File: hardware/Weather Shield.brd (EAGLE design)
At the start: 53.3 x 59.7 mm, 44 parts, among them Q1 BSS138, Q2 BSS138, U1 ARDUINO_R3_SHIELD, U2 3.3V MIC5219, U4 MPL3115A2LGA8, U5 HTU21D, U7 GP-635T, U8 TEMT6000

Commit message: Added analog sense on VIN/Batt level.
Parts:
- added R7: 1K, SparkFun:0603-RES
- added R8: 3.9K, SparkFun:0603-RES
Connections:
- new net BATT_LVL: R7.1, R8.2, U1.A2
- net GND: now also R7.2
- net RAW: now also R8.1
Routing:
- net BATT_LVL: track 0.00 -> 48.5 mm, vias 0 -> 1
- net RAW: track 42.1 -> 46.3 mm
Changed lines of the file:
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@@
 <element name="R16" library="SparkFun" package="0603-RES" value="1K" x="29.21" y="39.37" rot="R180"/>
 <element name="LOGO2" library="SparkFun-Aesthetics" package="SFE_LOGO_NAME_FLAME_.1" value="SFE_LOGO_NAME_FLAME.1_INCH" x="20.828" y="3.048"/>
+<element name="R7" library="SparkFun" package="0603-RES" value="1K" x="40.64" y="20.32" rot="R90"/>
+<element name="R8" library="SparkFun" package="0603-RES" value="3.9K" x="38.1" y="20.32" rot="R270"/>
 </elements>
 <signals>
@@
 <via x="30.48" y="34.29" extent="1-16" drill="0.508"/>
 <via x="21.59" y="27.94" extent="1-16" drill="0.508"/>
+<contactref element="R7" pad="2"/>
 </signal>
 <signal name="STAT2">
@@
 <wire x1="27.9701" y1="20" x2="30.16" y2="20" width="0.508" layer="1"/>
 <wire x1="30.16" y1="20" x2="30.61" y2="20.45" width="0.508" layer="1"/>
+<contactref element="R8" pad="1"/>
+<wire x1="34.29" y1="20.32" x2="35.56" y2="20.32" width="0.254" layer="1"/>
+<wire x1="38.1" y1="21.17" x2="36.41" y2="21.17" width="0.254" layer="1"/>
+<wire x1="36.41" y1="21.17" x2="35.56" y2="20.32" width="0.254" layer="1"/>
 </signal>
 <signal name="RXI">
@@
 <wire x1="30.06" y1="44.03" x2="33.02" y2="46.99" width="0.254" layer="1"/>
 </signal>
+<signal name="BATT_LVL">
+<contactref element="R8" pad="2"/>
+<contactref element="R7" pad="1"/>
+<contactref element="U1" pad="A2"/>
+<wire x1="50.8" y1="46.99" x2="52.07" y2="45.72" width="0.254" layer="16"/>
+<wire x1="52.07" y1="45.72" x2="52.07" y2="17.78" width="0.254" layer="16"/>
+<wire x1="52.07" y1="17.78" x2="50.8" y2="16.51" width="0.254" layer="16"/>
+<wire x1="50.8" y1="16.51" x2="39.37" y2="16.51" width="0.254" layer="16"/>
+<via x="39.37" y="16.51" extent="1-16" drill="0.508"/>
+<wire x1="39.37" y1="16.51" x2="39.37" y2="19.47" width="0.254" layer="1"/>
+<wire x1="39.37" y1="19.47" x2="40.64" y2="19.47" width="0.254" layer="1"/>
+<wire x1="39.37" y1="19.47" x2="38.1" y2="19.47" width="0.254" layer="1"/>
+</signal>
 </signals>

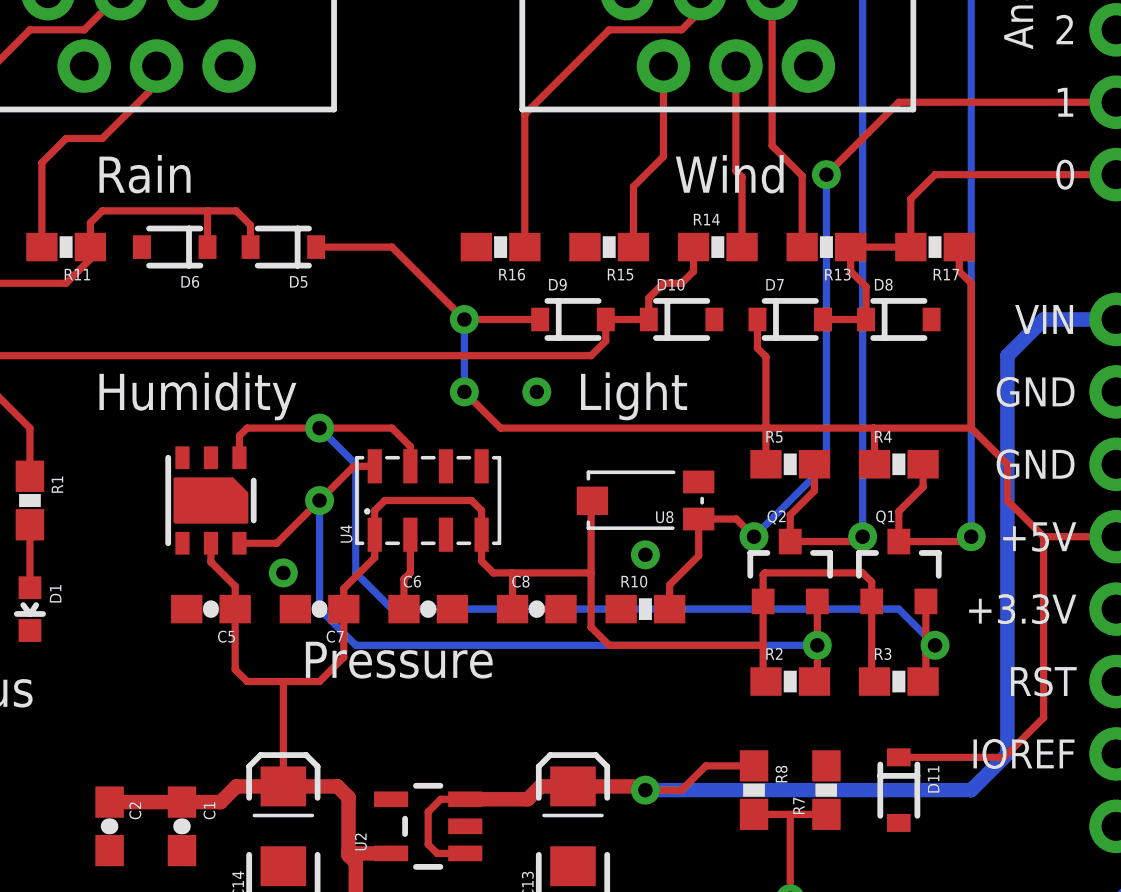
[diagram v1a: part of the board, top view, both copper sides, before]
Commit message: Reduction of ground plane around sensors.
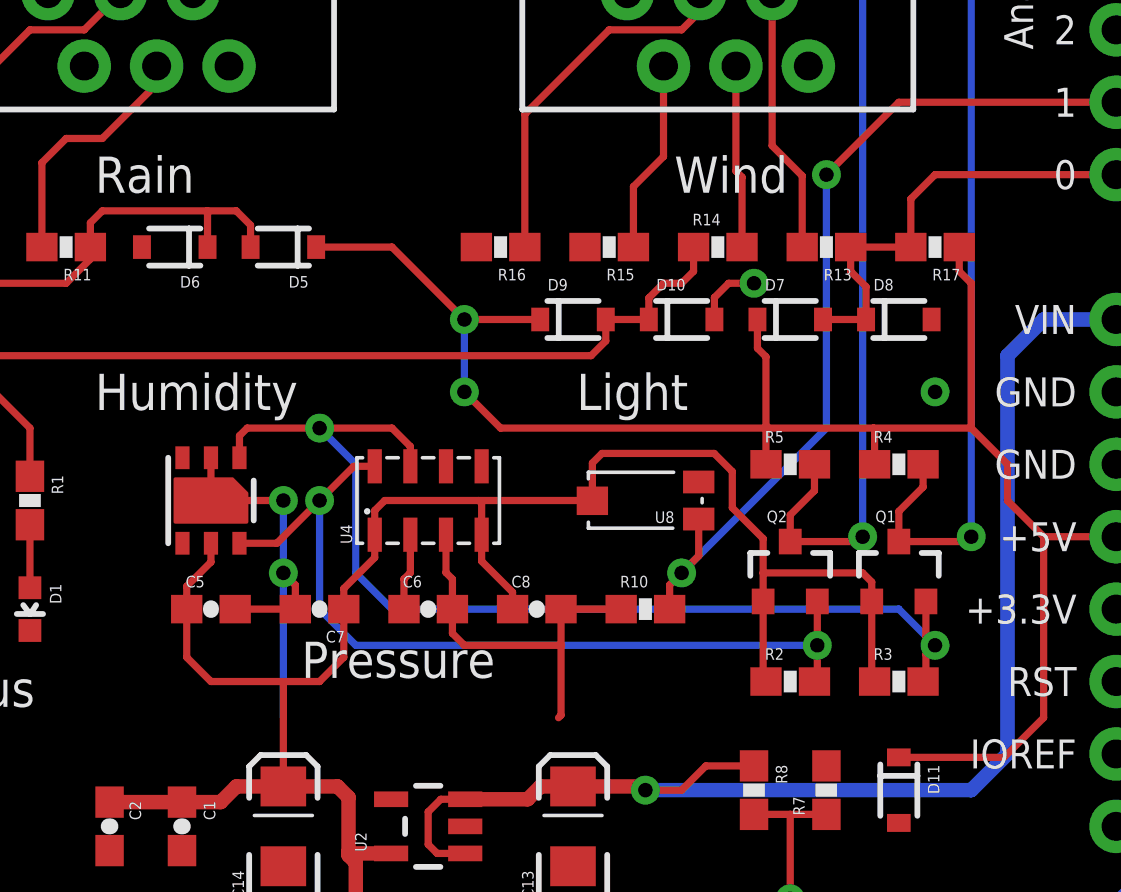
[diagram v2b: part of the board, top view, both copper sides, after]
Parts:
- turned C5 to 0 degrees
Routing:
- net GND: track 0.00 -> 31.1 mm, vias 3 -> 4
- net 3.3V: track 101.7 -> 104.0 mm
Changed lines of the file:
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@@
 <layer number="39" name="tKeepout" color="4" fill="11" visible="no" active="yes"/>
 <layer number="40" name="bKeepout" color="1" fill="11" visible="no" active="yes"/>
-<layer number="41" name="tRestrict" color="4" fill="10" visible="no" active="yes"/>
-<layer number="42" name="bRestrict" color="1" fill="10" visible="no" active="yes"/>
+<layer number="41" name="tRestrict" color="4" fill="10" visible="yes" active="yes"/>
+<layer number="42" name="bRestrict" color="1" fill="10" visible="yes" active="yes"/>
 <layer number="43" name="vRestrict" color="2" fill="10" visible="no" active="yes"/>
 <layer number="44" name="Drills" color="7" fill="1" visible="no" active="yes"/>
@@
 <text x="16.637" y="6.096" size="1.27" layer="21" ratio="15" rot="R90">Serial</text>
 <text x="28.575" y="0.635" size="1.524" layer="16" font="vector" ratio="20" rot="MR0">v10</text>
+<rectangle x1="13.97" y1="24.13" x2="40.64" y2="36.83" layer="41"/>
+<rectangle x1="13.97" y1="24.13" x2="40.64" y2="36.83" layer="42"/>
 </plain>
 <attributes>
@@
 <element name="C6" library="SparkFun" package="0603-CAP" value="0.1uF" x="26.67" y="26.67"/>
 <element name="C8" library="SparkFun" package="0603-CAP" value="1uF" x="30.48" y="26.67"/>
-<element name="C5" library="SparkFun" package="0603-CAP" value="0.1uF" x="19.05" y="26.67" rot="R180"/>
+<element name="C5" library="SparkFun" package="0603-CAP" value="0.1uF" x="19.05" y="26.67"/>
 <element name="U5" library="SparkFun-Sensors" package="HTU21D" value="HTU21D" x="19.05" y="30.48" rot="R90"/>
 <element name="U7" library="SparkFun-Connectors" package="JST-6-SMD-VERT-1.0MM" value="GP-635T" x="50.8" y="8.89" rot="R270"/>
@@
 <contactref element="R16" pad="2"/>
 <contactref element="R12" pad="2"/>
-<via x="34.29" y="28.575" extent="1-16" drill="0.508"/>
-<via x="30.48" y="34.29" extent="1-16" drill="0.508"/>
+<via x="38.1" y="38.1" extent="1-16" drill="0.508"/>
 <via x="21.59" y="27.94" extent="1-16" drill="0.508"/>
 <contactref element="R7" pad="2"/>
+<wire x1="27.295" y1="29.28" x2="27.295" y2="27.95" width="0.254" layer="1"/>
+<wire x1="27.295" y1="27.95" x2="27.52" y2="27.725" width="0.254" layer="1"/>
+<wire x1="27.52" y1="26.67" x2="27.52" y2="27.725" width="0.254" layer="1"/>
+<wire x1="27.52" y1="26.67" x2="27.52" y2="25.82" width="0.254" layer="1"/>
+<wire x1="27.52" y1="25.82" x2="27.94" y2="25.4" width="0.254" layer="1"/>
+<wire x1="19.9" y1="26.67" x2="22.01" y2="26.67" width="0.254" layer="1"/>
+<wire x1="19.05" y1="31.98" x2="19.05" y2="30.48" width="0.254" layer="1"/>
+<wire x1="19.05" y1="30.48" x2="21.59" y2="30.48" width="0.254" layer="1"/>
+<via x="21.59" y="30.48" extent="1-16" drill="0.508"/>
+<wire x1="22.01" y1="26.67" x2="22.01" y2="27.52" width="0.254" layer="1"/>
+<wire x1="22.01" y1="27.52" x2="21.59" y2="27.94" width="0.254" layer="1"/>
+<wire x1="21.59" y1="27.94" x2="21.59" y2="22.86" width="0.254" layer="16"/>
+<wire x1="21.59" y1="30.48" x2="21.59" y2="27.94" width="0.254" layer="16"/>
+<via x="44.45" y="34.29" extent="1-16" drill="0.508"/>
+<wire x1="36.71" y1="36.83" x2="36.71" y2="37.599" width="0.254" layer="1"/>
+<wire x1="36.71" y1="37.599" x2="37.211" y2="38.1" width="0.254" layer="1"/>
+<wire x1="37.211" y1="38.1" x2="38.1" y2="38.1" width="0.254" layer="1"/>
+<wire x1="31.33" y1="26.67" x2="31.33" y2="25.4" width="0.254" layer="1"/>
+<wire x1="31.33" y1="25.4" x2="31.33" y2="22.948" width="0.254" layer="1"/>
+<wire x1="31.33" y1="22.948" x2="31.242" y2="22.86" width="0.254" layer="1"/>
+<wire x1="27.94" y1="25.4" x2="31.33" y2="25.4" width="0.254" layer="1"/>
+<wire x1="31.33" y1="26.67" x2="33.44" y2="26.67" width="0.254" layer="1"/>
 </signal>
 <signal name="STAT2">
@@
 <wire x1="42.23" y1="26.94" x2="42.23" y2="24.23" width="0.254" layer="1"/>
 <wire x1="42.23" y1="24.23" x2="42.33" y2="24.13" width="0.254" layer="1"/>
-<wire x1="38.42" y1="26.94" x2="38.42" y2="25.4" width="0.254" layer="1"/>
-<wire x1="38.42" y1="25.4" x2="38.42" y2="24.23" width="0.254" layer="1"/>
+<wire x1="38.42" y1="26.94" x2="38.42" y2="24.23" width="0.254" layer="1"/>
 <wire x1="38.42" y1="24.23" x2="38.52" y2="24.13" width="0.254" layer="1"/>
-<wire x1="38.42" y1="26.94" x2="38.42" y2="27.879" width="0.254" layer="1"/>
 <wire x1="41.91" y1="27.94" x2="42.23" y2="27.62" width="0.254" layer="1"/>
 <wire x1="42.23" y1="26.94" x2="42.23" y2="27.62" width="0.254" layer="1"/>
@@
 <wire x1="25.3699" y1="18.1" x2="23.937" y2="18.1" width="0.508" layer="1"/>
 <wire x1="23.937" y1="18.1" x2="23.876" y2="18.161" width="0.508" layer="1"/>
-<wire x1="19.9" y1="26.67" x2="19.9" y2="24.55" width="0.254" layer="1"/>
-<wire x1="19.9" y1="24.55" x2="20.32" y2="24.13" width="0.254" layer="1"/>
 <wire x1="21.59" y1="24.13" x2="21.59" y2="20.45" width="0.254" layer="1"/>
-<wire x1="19.05" y1="28.98" x2="19.05" y2="28.321" width="0.254" layer="1"/>
-<wire x1="38.481" y1="27.94" x2="41.91" y2="27.94" width="0.254" layer="1"/>
-<wire x1="38.42" y1="27.879" x2="38.481" y2="27.94" width="0.254" layer="1"/>
-<wire x1="29.63" y1="26.67" x2="29.63" y2="27.901" width="0.254" layer="1"/>
-<wire x1="29.63" y1="27.901" x2="29.591" y2="27.94" width="0.254" layer="1"/>
 <wire x1="24.795" y1="29.28" x2="24.795" y2="28.478" width="0.254" layer="1"/>
 <wire x1="24.795" y1="28.478" x2="23.71" y2="27.393" width="0.254" layer="1"/>
@@
 <wire x1="23.71" y1="24.98" x2="22.86" y2="24.13" width="0.254" layer="1"/>
 <wire x1="22.86" y1="24.13" x2="21.59" y2="24.13" width="0.254" layer="1"/>
-<wire x1="21.59" y1="24.13" x2="20.32" y2="24.13" width="0.254" layer="1"/>
-<wire x1="19.9" y1="26.67" x2="19.9" y2="27.471" width="0.254" layer="1"/>
-<wire x1="19.9" y1="27.471" x2="19.05" y2="28.321" width="0.254" layer="1"/>
 <wire x1="28.545" y1="29.28" x2="28.545" y2="28.351" width="0.254" layer="1"/>
-<wire x1="28.545" y1="28.351" x2="28.956" y2="27.94" width="0.254" layer="1"/>
-<wire x1="28.956" y1="27.94" x2="29.591" y2="27.94" width="0.254" layer="1"/>
-<wire x1="28.545" y1="29.28" x2="28.545" y2="30.129" width="0.254" layer="1"/>
-<wire x1="28.545" y1="30.129" x2="28.194" y2="30.48" width="0.254" layer="1"/>
-<wire x1="28.194" y1="30.48" x2="25.146" y2="30.48" width="0.254" layer="1"/>
 <wire x1="25.146" y1="30.48" x2="24.795" y2="30.129" width="0.254" layer="1"/>
 <wire x1="24.795" y1="29.28" x2="24.795" y2="30.129" width="0.254" layer="1"/>
-<wire x1="32.385" y1="26.035" x2="33.02" y2="25.4" width="0.254" layer="1"/>
-<wire x1="33.02" y1="25.4" x2="38.42" y2="25.4" width="0.254" layer="1"/>
-<wire x1="29.591" y1="27.94" x2="32.385" y2="27.94" width="0.254" layer="1"/>
-<wire x1="32.385" y1="26.035" x2="32.385" y2="27.94" width="0.254" layer="1"/>
-<wire x1="32.385" y1="27.94" x2="32.385" y2="30.425" width="0.254" layer="1"/>
-<wire x1="32.385" y1="30.425" x2="32.43" y2="30.47" width="0.254" layer="1"/>
+<wire x1="18.2" y1="26.67" x2="18.2" y2="24.98" width="0.254" layer="1"/>
+<wire x1="18.2" y1="24.98" x2="19.05" y2="24.13" width="0.254" layer="1"/>
+<wire x1="19.05" y1="24.13" x2="21.59" y2="24.13" width="0.254" layer="1"/>
+<wire x1="19.05" y1="28.98" x2="19.05" y2="28.321" width="0.254" layer="1"/>
+<wire x1="18.2" y1="26.67" x2="18.2" y2="27.471" width="0.254" layer="1"/>
+<wire x1="18.2" y1="27.471" x2="19.05" y2="28.321" width="0.254" layer="1"/>
+<wire x1="41.91" y1="27.94" x2="38.42" y2="27.94" width="0.254" layer="1"/>
+<wire x1="29.63" y1="26.67" x2="29.63" y2="27.266" width="0.254" layer="1"/>
+<wire x1="29.63" y1="27.266" x2="28.545" y2="28.351" width="0.254" layer="1"/>
+<wire x1="25.146" y1="30.48" x2="28.448" y2="30.48" width="0.254" layer="1"/>
+<wire x1="28.448" y1="30.48" x2="32.42" y2="30.48" width="0.254" layer="1"/>
+<wire x1="32.42" y1="30.48" x2="32.43" y2="30.47" width="0.254" layer="1"/>
+<wire x1="28.545" y1="29.28" x2="28.545" y2="30.383" width="0.254" layer="1"/>
+<wire x1="28.545" y1="30.383" x2="28.448" y2="30.48" width="0.254" layer="1"/>
+<wire x1="32.43" y1="30.47" x2="32.43" y2="31.795" width="0.254" layer="1"/>
+<wire x1="32.43" y1="31.795" x2="32.766" y2="32.131" width="0.254" layer="1"/>
+<wire x1="32.766" y1="32.131" x2="36.703" y2="32.131" width="0.254" layer="1"/>
+<wire x1="36.703" y1="32.131" x2="37.338" y2="31.496" width="0.254" layer="1"/>
+<wire x1="37.338" y1="31.496" x2="37.338" y2="30.226" width="0.254" layer="1"/>
+<wire x1="38.42" y1="26.94" x2="38.42" y2="27.94" width="0.254" layer="1"/>
+<wire x1="38.42" y1="27.94" x2="38.42" y2="29.144" width="0.254" layer="1"/>
+<wire x1="38.42" y1="29.144" x2="37.338" y2="30.226" width="0.254" layer="1"/>
 </signal>
 <signal name="SCL">
@@
 <wire x1="43.18" y1="44.45" x2="40.64" y2="41.91" width="0.254" layer="1"/>
 <via x="40.64" y="41.91" extent="1-16" drill="0.508"/>
-<wire x1="40.64" y1="41.91" x2="40.64" y2="31.75" width="0.254" layer="16"/>
-<wire x1="40.64" y1="31.75" x2="38.1" y2="29.21" width="0.254" layer="16"/>
-<wire x1="36.16" y1="29.83" x2="37.48" y2="29.83" width="0.254" layer="1"/>
-<wire x1="37.48" y1="29.83" x2="38.1" y2="29.21" width="0.254" layer="1"/>
-<via x="38.1" y="29.21" extent="1-16" drill="0.508"/>
+<wire x1="40.64" y1="41.91" x2="40.64" y2="33.02" width="0.254" layer="16"/>
+<wire x1="40.64" y1="33.02" x2="35.56" y2="27.94" width="0.254" layer="16"/>
+<via x="35.56" y="27.94" extent="1-16" drill="0.508"/>
 <wire x1="36.16" y1="29.83" x2="36.16" y2="28.54" width="0.254" layer="1"/>
-<wire x1="36.16" y1="28.54" x2="35.14" y2="27.52" width="0.254" layer="1"/>
+<wire x1="36.16" y1="28.54" x2="35.56" y2="27.94" width="0.254" layer="1"/>
 <wire x1="35.14" y1="26.67" x2="35.14" y2="27.52" width="0.254" layer="1"/>
+<wire x1="35.14" y1="27.52" x2="35.56" y2="27.94" width="0.254" layer="1"/>
 </signal>
 <signal name="PWR_CTL">
@@
 </signal>
 </signals>
+<errors>
+</errors>
 </board>
 </drawing>
